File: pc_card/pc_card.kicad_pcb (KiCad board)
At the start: 2 copper layers, 64.8 x 47.5 mm, 44 parts, among them IC1 SV 3.3V, IC2 74LVC1G00, IC3 SV 4.5V, IC4 TPA152DR, J1 PCMCIA Connector, J2 L R G, U1 Z8601720ASG, U2 25LCxxx, U3 YMF289B-S, U4 YAC516-E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

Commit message: fixes
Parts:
- removed D1: Generic 250mA, Diode_SMD:D_SOD-323_HandSoldering
- removed IC2: 74LVC1G00, Package_TO_SOT_SMD:SOT-23-5_HandSoldering
- removed JP3: RW RO, Jumper:SolderJumper-3_P1.3mm_Bridged12_RoundedPad1.0x1.5mm_NumberLabels
- removed RN1: 20k, Resistor_SMD:R_Array_Convex_4x1206
- added R12: EEPROM, Resistor_SMD:R_0603_1608Metric_Pad0.98x0.95mm_HandSolder, F.Cu at (135.4, 64.0)
- added R3: 20k, Resistor_SMD:R_0805_2012Metric_Pad1.20x1.40mm_HandSolder, F.Cu at (158.8, 79.6)
- added R5: 20k, Resistor_SMD:R_0805_2012Metric_Pad1.20x1.40mm_HandSolder, F.Cu at (160.8, 79.6)
- added R6: 20k, Resistor_SMD:R_0805_2012Metric_Pad1.20x1.40mm_HandSolder, F.Cu at (156.5, 79.6)
- added R7: 20k, Resistor_SMD:R_0805_2012Metric_Pad1.20x1.40mm_HandSolder, F.Cu at (154.4, 79.6)
- J2: value L R G -> Headphones Out
- U1: footprint Package_QFP:VQFP-100_14x14mm_P0.5mm -> Package_QFP:LQFP-100_14x14mm_P0.5mm
- U2: value 25LCxxx -> 93AAxxC
- moved U2 1.56 mm to (140.2, 63.0), turned to 180 degrees
- moved IC4 0.13 mm to (156.2, 71.5)
- turned C11 to 90 degrees
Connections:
- J1 pad 10: (no net) -> unconnected-(J1-A11-Pad10)
- J1 pad 13: (no net) -> unconnected-(J1-A13-Pad13)
- J1 pad 14: (no net) -> unconnected-(J1-A14-Pad14)
- J1 pad 18: (no net) -> unconnected-(J1-VPP-Pad18)
- J1 pad 19: (no net) -> unconnected-(J1-A16-Pad19)
- J1 pad 20: (no net) -> unconnected-(J1-A15-Pad20)
- J1 pad 21: (no net) -> unconnected-(J1-A12-Pad21)
- J1 pad 46: (no net) -> unconnected-(J1-A17-Pad46)
- J1 pad 47: (no net) -> unconnected-(J1-A18-Pad47)
- J1 pad 48: (no net) -> unconnected-(J1-A19-Pad48)
- J1 pad 49: (no net) -> unconnected-(J1-A20-Pad49)
- J1 pad 50: (no net) -> unconnected-(J1-A21-Pad50)
- J1 pad 52: (no net) -> unconnected-(J1-VPP-Pad52)
- J1 pad 53: (no net) -> unconnected-(J1-A22-Pad53)
- J1 pad 54: (no net) -> unconnected-(J1-A23-Pad54)
- J1 pad 55: (no net) -> unconnected-(J1-A24-Pad55)
- J1 pad 56: (no net) -> unconnected-(J1-A25-Pad56)
- U1 pad 13: (no net) -> unconnected-(U1-ATA_DATA8/RES1-Pad13)
- U1 pad 17: (no net) -> unconnected-(U1-ATA_DATA9/PACK_IN-Pad17)
- U1 pad 19: (no net) -> unconnected-(U1-ATA_DATA10-Pad19)
- U1 pad 22: (no net) -> unconnected-(U1-ATA_DATA11-Pad22)
- U1 pad 25: (no net) -> unconnected-(U1-ATA_DATA12-Pad25)
- U1 pad 27: (no net) -> unconnected-(U1-ATA_DATA13-Pad27)
- U1 pad 29: (no net) -> unconnected-(U1-ATA_DATA14-Pad29)
- U1 pad 31: (no net) -> unconnected-(U1-ATA_DATA15-Pad31)
- U1 pad 35: (no net) -> unconnected-(U1-ATA_IOCHRDY-Pad35)
- U1 pad 41: (no net) -> unconnected-(U1-ATA_HA2-Pad41)
- U1 pad 43: (no net) -> unconnected-(U1-~{ATA}_HCS1-Pad43)
- U1 pad 45: (no net) -> unconnected-(U1-~{ATA}_PDIAG/ATA_BHE/RING_IN-Pad45)
- U1 pad 46: (no net) -> unconnected-(U1-~{ATA}_PDASP/EXTP_WP-Pad46)
- U1 pad 47: (no net) -> unconnected-(U1-~{ATA}_DACK/BVD2-Pad47)
- U1 pad 49: (no net) -> unconnected-(U1-~{ATA}_MRD-Pad49)
- U1 pad 55: (no net) -> unconnected-(U1-~{ATA}_MWR-Pad55)
- U1 pad 57: (no net) -> unconnected-(U1-M_PINT-Pad57)
- U1 pad 59: (no net) -> unconnected-(U1-EXTP_PWDN-Pad59)
- U1 pad 60: (no net) -> unconnected-(U1-EXTP_AUDIO-Pad60)
- U1 pad 61: (no net) -> unconnected-(U1-EXTP_STSCHG/RES2-Pad61)
- U2 pad 1: CS# -> EE_CS
- U2 pad 2: EE_DI -> EE_SK
- U2 pad 3: WP# -> EE_DO
- U2 pad 4: AGND -> EE_DI
- U2 pad 5: EE_DO -> AGND
- U2 pad 6: EE_SK -> unconnected-(U2-ORG-Pad6)
- U2 pad 7: VPP -> unconnected-(U2-NC-Pad7)
- U3 pad 27: (no net) -> unconnected-(U3-/TEST1-Pad27)
- U3 pad 29: (no net) -> unconnected-(U3-/TEST2-Pad29)
- U3 pad 31: (no net) -> unconnected-(U3-/TEST3-Pad31)
- U3 pad 34: (no net) -> unconnected-(U3-WCO-Pad34)
- U4 pad 1: (no net) -> unconnected-(U4-TST1-Pad1)
- U4 pad 24: (no net) -> unconnected-(U4-TST2-Pad24)
- Y2 pad 2: (no net) -> unconnected-(Y2-Pad2)
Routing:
- net AGND: track 197.6 -> 234.9 mm, vias 74 -> 80
- net VPP: track 21.2 -> 2.41 mm, vias 2 -> 0
- net WP#: track 11.5 -> 0.00 mm, vias 1 -> 0
- net CS#: track 10.5 -> 0.00 mm
- net VCC: track 270.5 -> 281.0 mm, vias 17 -> 28
- net EE_CS: track 20.1 -> 10.8 mm, vias 2 -> 0
- net EE_DO: track 6.99 -> 14.1 mm
- net EE_SK: track 8.24 -> 15.1 mm
- net AOTR: track 14.5 -> 18.9 mm
- net Net-(C13-Pad1): track 4.62 -> 2.04 mm
- net Net-(C11-Pad1): track 4.62 -> 2.44 mm
- net Net-(IC4-IN2-): track 15.2 -> 16.3 mm
- net Net-(IC4-VO1): track 24.8 -> 25.7 mm
- net Net-(IC4-IN1-): track 10.3 -> 10.9 mm
- net POR#: track 29.8 -> 29.2 mm
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- added copper zone on In1.Cu, net AGND
- added copper zone on In2.Cu, net AGND
- added copper zone on In2.Cu, net AVDD
- added copper zone on In2.Cu, net VCC
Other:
- copper layers 2 -> 4
- board text added: "Card Barker OPL3 PCMCIA PC Card Prototype One tilde.gay/~ai/cardbarker"
- board text removed: "Card Barker OPL3 Sound Card PCMCIA PC Card Prototype One yottatsa.name/cardbarker"

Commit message: devboard; finishing 4L card
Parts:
- added R13: ORG, Resistor_SMD:R_0603_1608Metric_Pad0.98x0.95mm_HandSolder, F.Cu at (135.2, 61.4)
- added TP3: CS, TestPoint:TestPoint_Keystone_5015_Micro-Minature, B.Cu at (138.9, 79.1)
- added TP4: GND, TestPoint:TestPoint_Pad_D1.0mm, B.Cu at (157.7, 85.0)
- added TP5: RESET, TestPoint:TestPoint_Keystone_5015_Micro-Minature, B.Cu at (148.8, 79.1)
- added TP6: PWDN, TestPoint:TestPoint_Keystone_5015_Micro-Minature, B.Cu at (130.0, 74.5)
- added TP7: AUDIO, TestPoint:TestPoint_Keystone_5015_Micro-Minature, B.Cu at (130.0, 70.0)
- added TP8: 5V/~{3V}, TestPoint:TestPoint_Keystone_5015_Micro-Minature, B.Cu at (148.8, 93.3)
- R10: footprint Resistor_SMD:R_0402_1005Metric_Pad0.72x0.64mm_HandSolder -> Resistor_SMD:R_0603_1608Metric_Pad0.98x0.95mm_HandSolder
- R11: footprint Resistor_SMD:R_1206_3216Metric_Pad1.30x1.75mm_HandSolder -> Resistor_SMD:R_0603_1608Metric_Pad0.98x0.95mm_HandSolder
- U2: value 93AAxxC -> 93CxxC
- moved R11 3.56 mm to (143.8, 82.4), turned to 90 degrees
- moved R12 1.19 mm to (135.2, 65.1), turned to 90 degrees
- moved R10 0.08 mm to (138.9, 92.8)
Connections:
- net YMFVS renamed 5V/~{3V}
- U1 pad 59: unconnected-(U1-EXTP_PWDN-Pad59) -> Net-(U1-EXTP_PWDN)
- U1 pad 60: unconnected-(U1-EXTP_AUDIO-Pad60) -> Net-(U1-EXTP_AUDIO)
- U2 pad 6: unconnected-(U2-ORG-Pad6) -> Net-(U2-ORG)
- U2 pad 7: unconnected-(U2-NC-Pad7) -> AGND
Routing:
- net AGND: track 234.9 -> 225.9 mm, vias 80 -> 116
- net IIRQ#: track 51.3 -> 44.7 mm
- net 5V/~{3V}: track 12.6 -> 19.1 mm, vias 0 -> 1
- net Net-(U1-EXTP_PWDN): track 0.00 -> 6.33 mm, vias 0 -> 1
- net ICS0#: track 53.7 -> 59.7 mm
- net Net-(U1-EXTP_AUDIO): track 0.00 -> 5.90 mm, vias 0 -> 1
- net POR#: track 29.2 -> 25.3 mm
- net AVDD: track 158.2 -> 155.0 mm
- net ATA_HRESET#: track 55.0 -> 51.8 mm
- net Net-(U2-ORG): track 0.00 -> 2.58 mm
- net IWR#: track 44.6 -> 42.5 mm
- net VCC: track 281.0 -> 282.8 mm
- net VCOM: track 15.9 -> 14.2 mm, vias 2 -> 0
- net D12: track 31.7 -> 30.3 mm
- net Net-(IC4-IN1-): track 10.9 -> 9.55 mm
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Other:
- board text added: "Card Barker OPL3 PCMCIA PC Card tilde.gay/~ai/cardbarker"
- board text added: "HW rev.2"
- board text removed: "Card Barker OPL3 PCMCIA PC Card Prototype One tilde.gay/~ai/cardbarker"

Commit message: ground reshuffle
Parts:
- moved TP5 11.5 mm to (139.1, 73.0)
- moved IC1 6.91 mm to (143.1, 71.2), turned to 90 degrees
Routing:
- net AGND: track 225.9 -> 217.7 mm, vias 116 -> 120
- net POR#: track 25.3 -> 17.5 mm
- net VCC: track 282.8 -> 279.2 mm, vias 28 -> 32

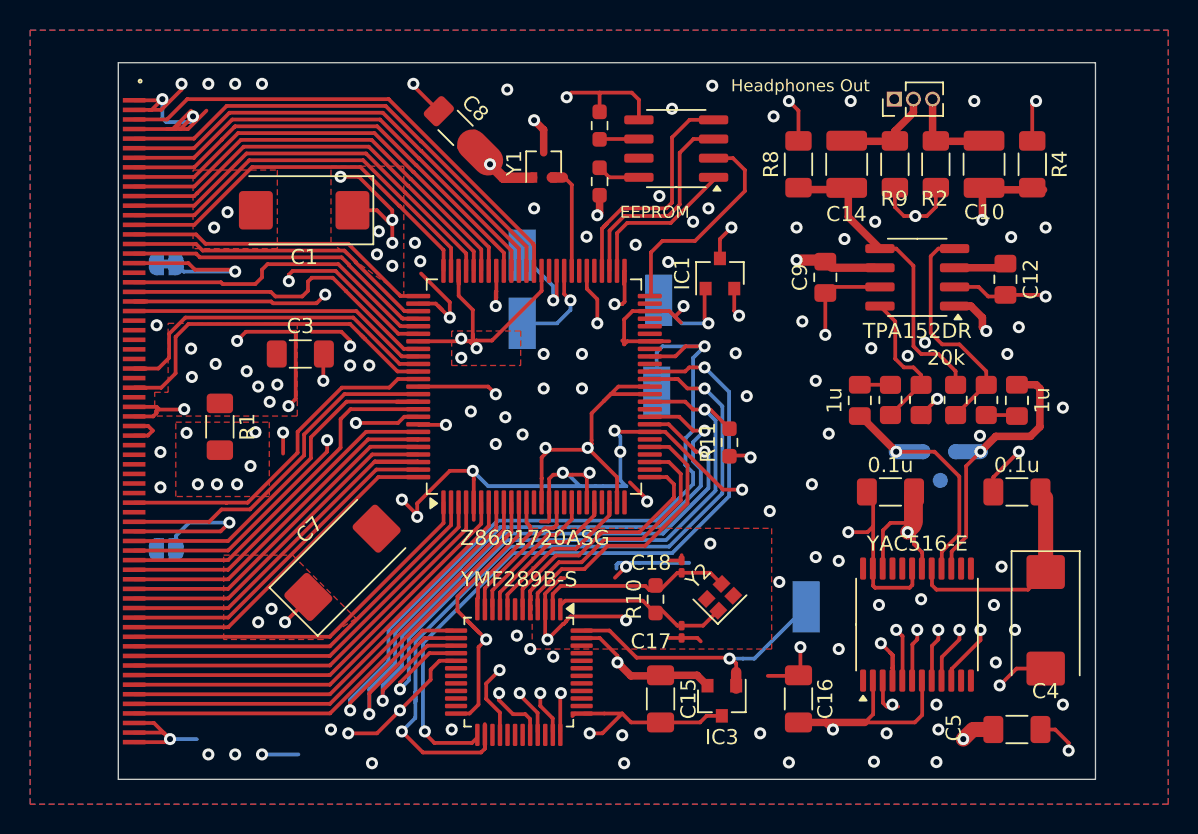
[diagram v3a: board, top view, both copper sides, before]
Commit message: card hw rev 2 to manufacture
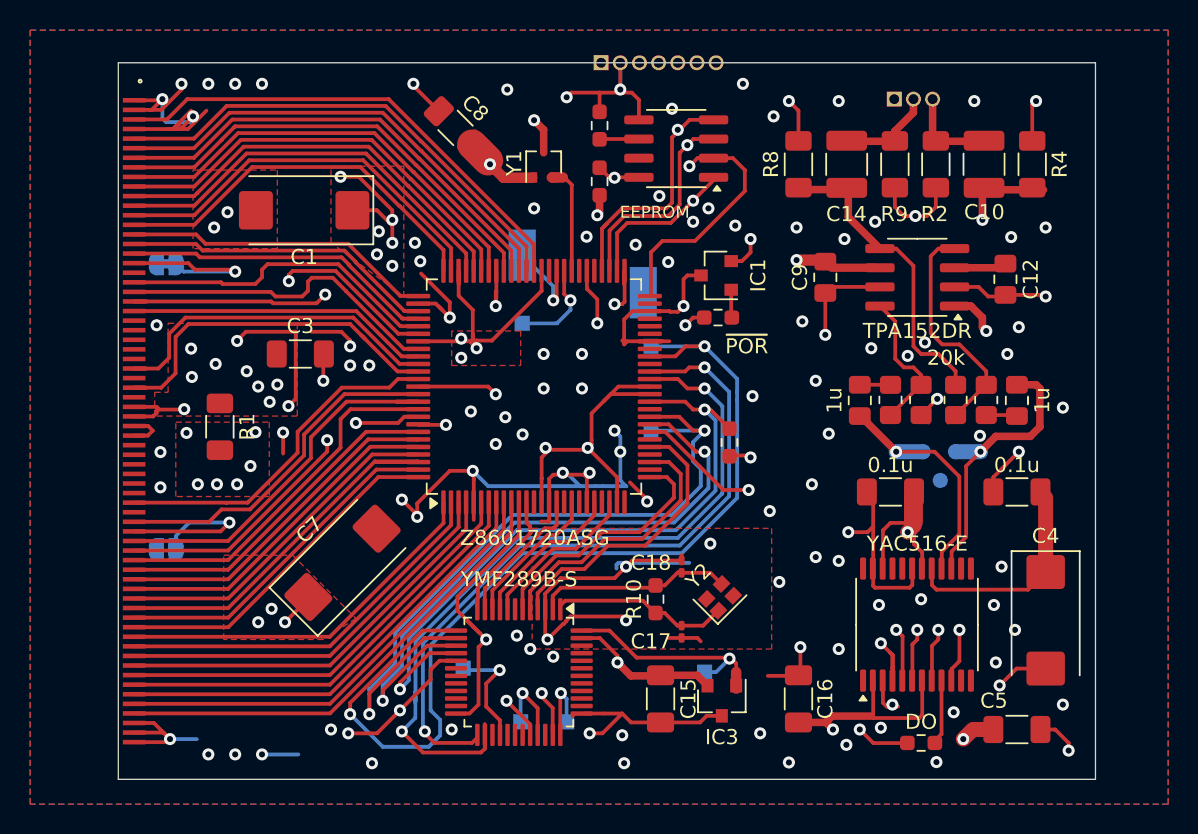
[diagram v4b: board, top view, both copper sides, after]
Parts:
- added J3: SPI, Connector_PinHeader_1.27mm:PinHeader_1x07_P1.27mm_Vertical, F.Cu at (135.3, 57.3)
- added R14: DO, Resistor_SMD:R_0603_1608Metric_Pad0.98x0.95mm_HandSolder, F.Cu at (156.5, 102.4)
- added R15: ~{POR}, Resistor_SMD:R_0603_1608Metric_Pad0.98x0.95mm_HandSolder, F.Cu at (143.0, 74.2)
- added TP10: ~{RD}, TestPoint:TestPoint_Pad_1.0x1.0mm, B.Cu at (138.6, 81.7)
- added TP11: CK, TestPoint:TestPoint_Pad_1.0x1.0mm, B.Cu at (133.0, 101.0)
- added TP12: ~{PD}, TestPoint:TestPoint_Pad_1.0x1.0mm, B.Cu at (126.1, 97.4)
- added TP9: DO, TestPoint:TestPoint_Pad_1.0x1.0mm, B.Cu at (129.9, 101.0)
- J2: moved to B.Cu
- R11: value 20k -> IRQ
- TP3: value CS -> ~{CS}; footprint TestPoint:TestPoint_Keystone_5015_Micro-Minature -> TestPoint:TestPoint_Pad_1.0x1.0mm
- TP5: value RESET -> GND
- TP6, TP8: footprint TestPoint:TestPoint_Keystone_5015_Micro-Minature -> TestPoint:TestPoint_Pad_1.0x1.0mm
- moved TP8 8.00 mm to (142.1, 97.7)
- moved TP3 3.07 mm to (138.6, 76.1)
- moved TP5 1.14 mm to (138.0, 72.5), turned to 90 degrees
- moved IC1 0.28 mm to (142.9, 71.4), turned to 180 degrees
- turned J2 to -90 degrees
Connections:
- IC1 pad 1: POR# -> Net-(IC1-~{RST})
- TP5 pad 1: POR# -> AGND
- U3 pad 33: DO -> Net-(U3-DO)
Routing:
- net Net-(U3-DO): track 0.00 -> 38.0 mm, vias 0 -> 2
- net DO: track 38.7 -> 4.38 mm, vias 2 -> 0
- net POR#: track 17.5 -> 30.1 mm
- net AGND: track 217.7 -> 228.7 mm, vias 120 -> 119
- net EE_CS: track 10.5 -> 20.5 mm, vias 0 -> 1
- net EE_SK: track 14.6 -> 24.2 mm, vias 0 -> 1
- net VPP: track 2.87 -> 10.4 mm, vias 0 -> 1
- net EE_DO: track 14.1 -> 20.3 mm, vias 0 -> 1
- net EE_DI: track 16.0 -> 22.0 mm, vias 0 -> 1
- net ICS0#: track 60.1 -> 65.7 mm
- net 5V/~{3V}: track 19.1 -> 14.7 mm
- net LRO: track 43.0 -> 38.7 mm
- net VCC: track 279.2 -> 275.0 mm
- net IRD#: track 47.1 -> 50.6 mm
- net DACPD: track 36.5 -> 39.0 mm
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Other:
- board text added: "GND R L"
- board text added: "VPP GND DI DO SK CS ~{RES}"
